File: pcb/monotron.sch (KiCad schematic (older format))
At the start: 29 parts, among them J1 USB_A, J2 USB_B_Micro, J3 SD_Card, J4 Mini-DIN-6, J5 Mini-DIN-6, J6 Conn_02x06_Odd_Even, J7 DB25_Female, J8 DB9_Male, U1 TPS73633DBV, U2 TM4C1231H6PM, Y1 16MHz, Y2 32kHz

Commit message: Added I/O, RS232 and VGA interfaces. Just audio to add.
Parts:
- removed J4, J5: Mini-DIN-6, symbol Connector:Mini-DIN-6
- removed J6: Conn_02x06_Odd_Even, symbol Connector_Generic:Conn_02x06_Odd_Even
- removed J7: DB25_Female, symbol Connector:DB25_Female
- added J5: Conn_02x06_Odd_Even, symbol Connector_Generic:Conn_02x06_Odd_Even
- added J6: DB15_Female_HighDensity_MountingHoles, symbol Connector:DB15_Female_HighDensity_MountingHoles
- added R1, R2, R3: 330, symbol Device:R
- renumbered J8 to J4
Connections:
- net labels added: PA2_SD_CLK, PA3_SD_CS, PA4_SD_MISO, PA5_SD_MOSI, PB4_VGA_HSYNC, PB5_VGA_VSYNC, PB7_VGA_GRN, PD3_VGA_BLU, PE4_AUD_L, PE5_AUD_R, PF1_VGA_RED
- net labels removed: KB_CLK, KB_DATA, MS_CLK, MS_DATA, PA2, PA3, PA4, PA5, PB4, PB5, PB7, PD3, PE4, PE5, PF1, SD_CLK, SD_CS, SD_MISO, SD_MOSI
- wire segments 234 -> 240
- no-connect marks 15 -> 38
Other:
- note added: "TODO! AUDIO OUTPUT GOES HERE"
- note removed: "PS/2 Keyboard"
- note removed: "PS/2 Mouse"
- note removed: "Printer"
- moved on the sheet: J4

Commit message: Changed to use Launchpad instead of bare chip. PS/2 handled by ATTINY24. LPT handled by MCP23017.
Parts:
- removed C1, C10, C17: 1.0u, symbol Device:C
- removed C11: 2.2u, symbol Device:C
- removed C12, C14, C16: 10n, symbol Device:C
- removed C13, C15, C8, C9: 100n, symbol Device:C
- removed C4: 10p, symbol Device:C
- removed C7: 24p, symbol Device:C
- removed J1: USB_A, symbol Connector:USB_A
- removed U1: TPS73633DBV, Package_TO_SOT_SMD:SOT-23-5, symbol Regulator_Linear:TPS73633DBV
- removed U2: TM4C1231H6PM, Package_QFP:LQFP-64_10x10mm_P0.5mm, symbol MCU_Texas:TM4C1231H6PM
- removed Y1: 16MHz, symbol Device:Crystal
- removed Y2: 32kHz, symbol Device:Crystal
- added C2: 10u, symbol Device:C
- added J1: Mono / Stereo, symbol Connector:Conn_01x03_Male
- added J2: AudioJack3, symbol Connector:AudioJack3
- added R1, R2: 150, symbol Device:R
- added R3, R4: 270, symbol Device:R
- added R5, R6: 4.7k, symbol Device:R
- added U2: TM4C123G_Launchpad, symbol tm4c123g_launchpad:TM4C123G_Launchpad
- C3: value 0.01u -> 10u
- C5: value 10p -> 33n
- C6: value 24p -> 33n
- renumbered C2 to C7, J4 to J3, J2 to J4, J3 to J5, J5 to J6, J6 to J7, R1 to R7, R2 to R8, R3 to R9
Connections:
- net labels added: +3V3, PA6_I2C_SCL, PA7_I2C_SDA, PD0_INT_B, PE0_INT_A
- net labels removed: +1V2, PA0, PA1, PA6, PA7, PB2, PB3, PB6, PC0, PC1, PC2, PC3, PD0, PD1, PD2, PD4_USB_DM, PD5_USB_DP, PE0, PE1, PE2, PE3, PE4_AUD_L, PE5_AUD_R, PF0, PF2, PF3, ~HIB, ~RST, ~WAKE
- wire segments 240 -> 145
- no-connect marks 38 -> 31
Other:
- note removed: "TODO! AUDIO OUTPUT GOES HERE"
- note removed: "USB Host Port"
- moved on the sheet: C7, J3, J4, J5, J6, J7, R7, R8, R9

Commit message: Adding footprints.
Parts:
- removed J4: USB_B_Micro, symbol Connector:USB_B_Micro
- added J3: Jack-DC, Connector_BarrelJack:BarrelJack_CUI_PJ-102AH_Horizontal, symbol Connector:Jack-DC
- C1: renamed from C2; footprint (none) -> Capacitor_THT:C_Radial_D5.0mm_H5.0mm_P2.00mm
- C2: renamed from C3; footprint (none) -> Capacitor_THT:C_Radial_D5.0mm_H5.0mm_P2.00mm
- C3: renamed from C7; footprint (none) -> Capacitor_THT:C_Radial_D5.0mm_H5.0mm_P2.00mm
- C4: renamed from C5; footprint (none) -> Capacitor_THT:C_Disc_D5.0mm_W2.5mm_P2.50mm
- C5: renamed from C6; footprint (none) -> Capacitor_THT:C_Disc_D5.0mm_W2.5mm_P2.50mm
- J1: footprint (none) -> Connector_PinHeader_2.54mm:PinHeader_1x03_P2.54mm_Vertical; Digikey (none) -> 609-3504-ND‎
- J4: renamed from J3; footprint (none) -> Connector_Dsub:DSUB-9_Male_Horizontal_P2.77x2.84mm_EdgePinOffset7.70mm_Housed_MountingHolesOffset9.12mm; Digikey (none) -> 609-5918-ND
- J5: footprint (none) -> Connector_Card:SD_TE_2041021; Digikey (none) -> A130907-ND‎
- J6: footprint (none) -> Connector_PinHeader_2.54mm:PinHeader_2x06_P2.54mm_Vertical; Digikey (none) -> 609-3263-ND‎
- J7: footprint (none) -> Connector_Dsub:DSUB-15-HD_Female_Horizontal_P2.29x1.98mm_EdgePinOffset8.35mm_Housed_MountingHolesOffset10.89mm; Digikey (none) -> 609-5181-ND
- R1, R2, R3, R4, R5, R6, R7, R8, R9: footprint (none) -> Resistor_THT:R_Axial_DIN0411_L9.9mm_D3.6mm_P12.70mm_Horizontal
- U1: renamed from U2; footprint (none) -> Launchpad:Launchpad_4x10
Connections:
- no-connect marks 31 -> 27
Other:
- moved on the sheet: C3

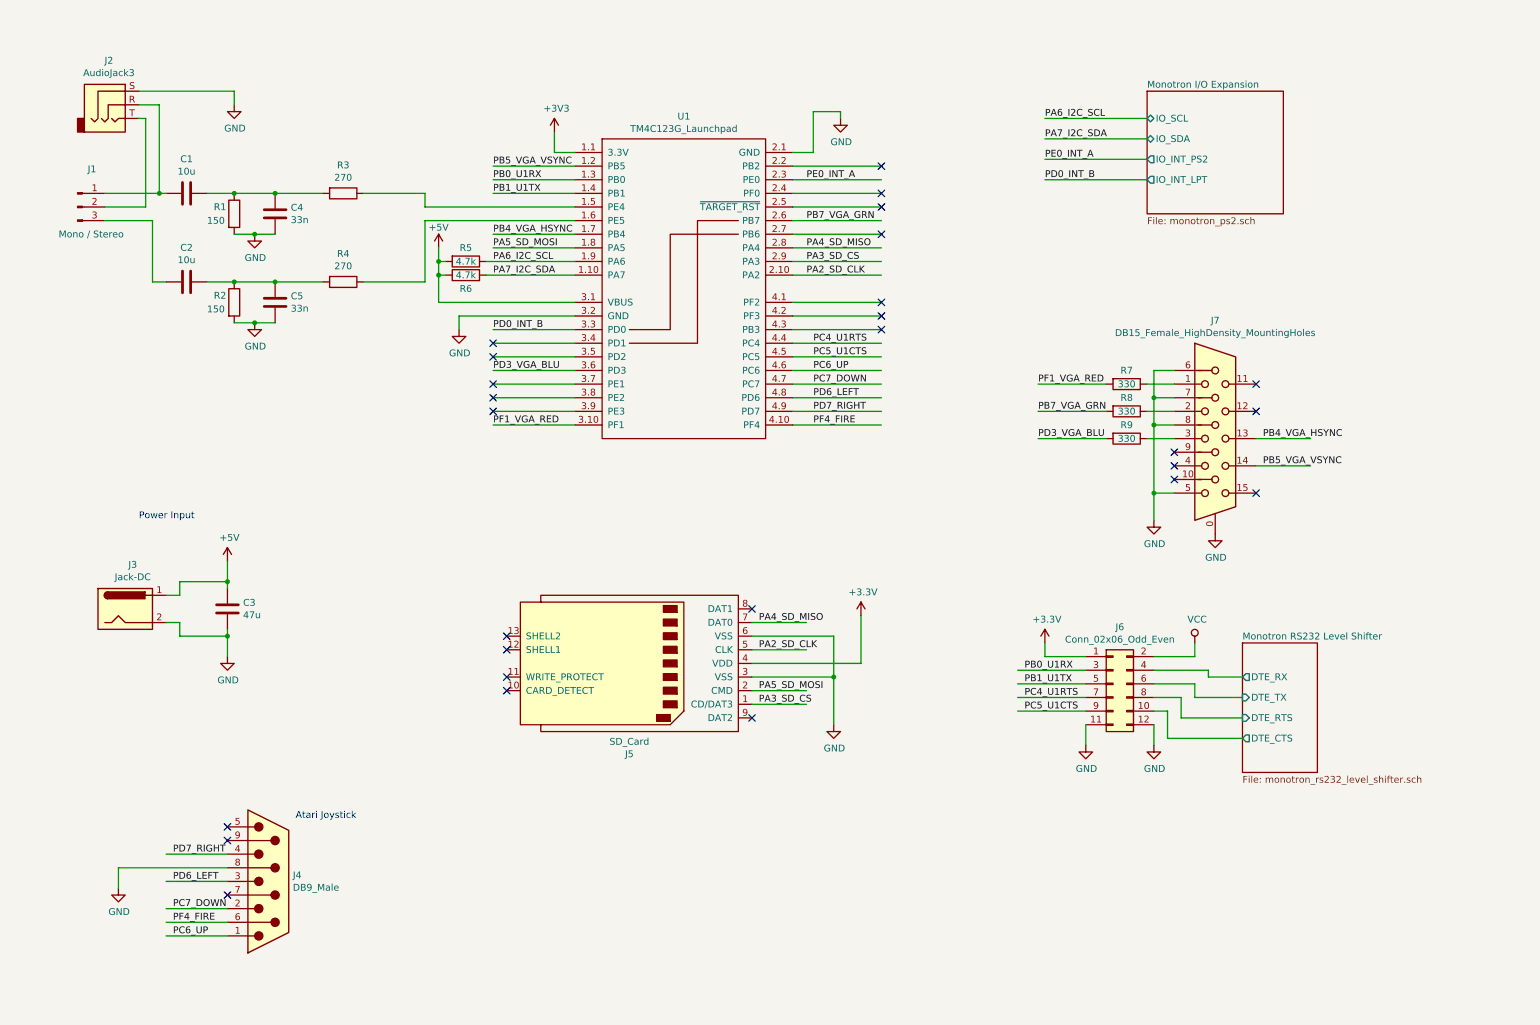
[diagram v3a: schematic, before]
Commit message: Added footprints. Change SD footprint for breakout board. Changed PS2/LPT interface to single AtMega48A. Moved MAX3232 to main sheet. Added I2C header. Started PCB layout.
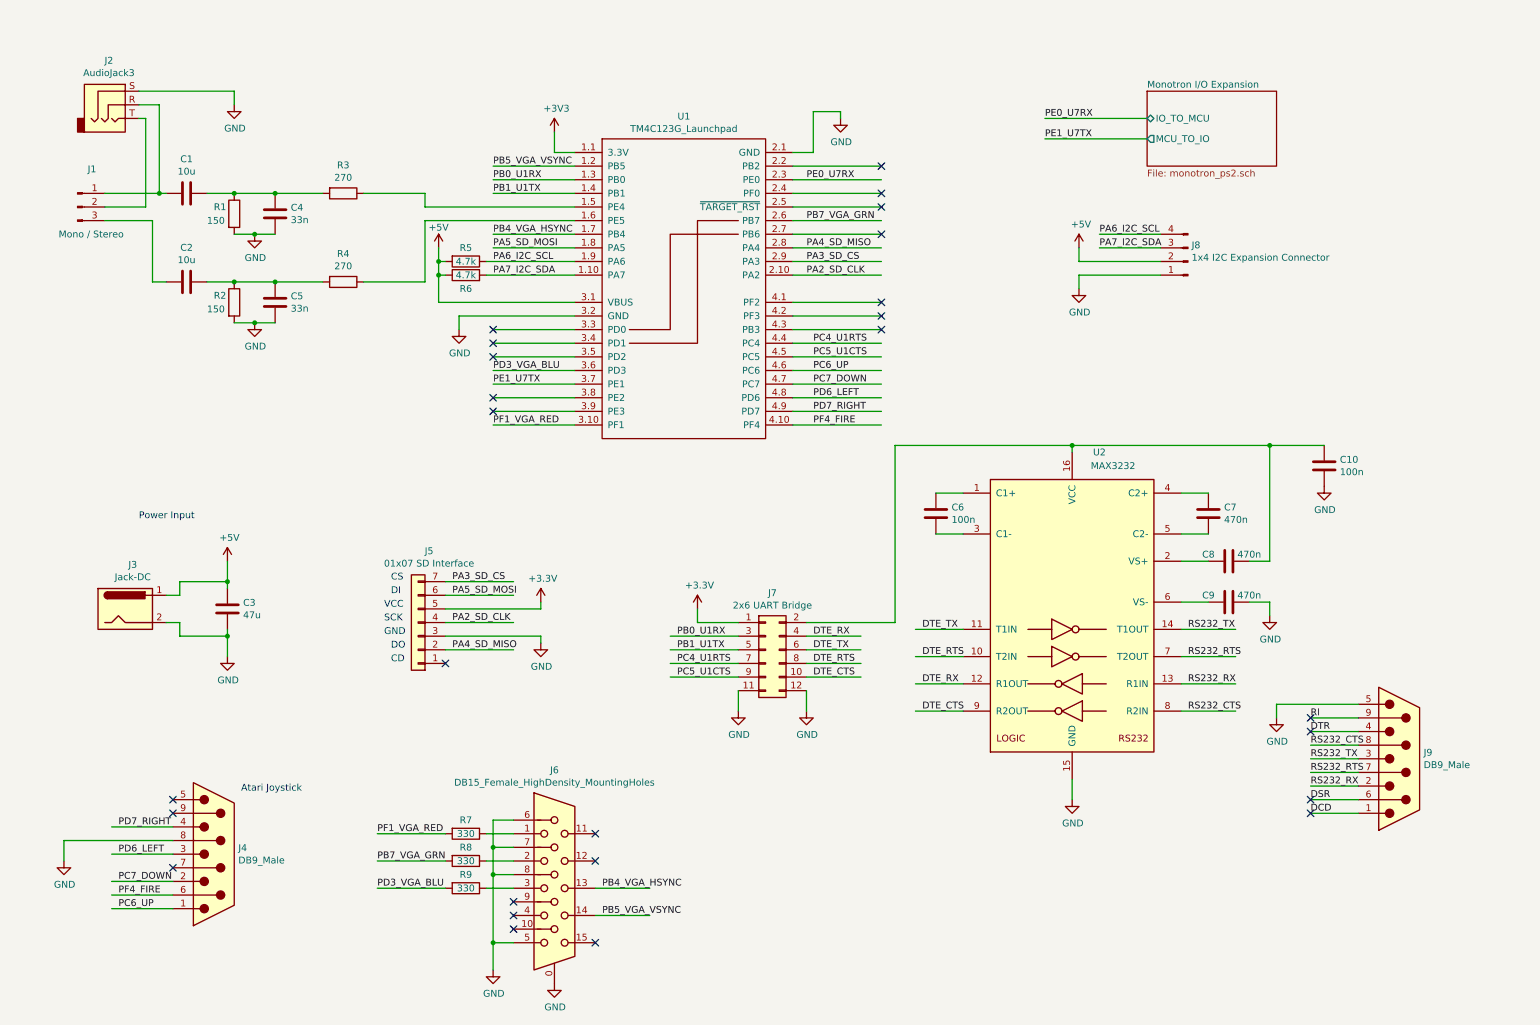
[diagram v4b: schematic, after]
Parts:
- removed J5: SD_Card, Connector_Card:SD_TE_2041021, symbol Connector:SD_Card
- added C10, C6: 100n, Capacitor_THT:C_Disc_D5.0mm_W2.5mm_P2.50mm, symbol Device:C
- added C7, C8, C9: 470n, Capacitor_THT:C_Disc_D5.0mm_W2.5mm_P2.50mm, symbol Device:C
- added J5: 01x07 SD Interface, Connector_PinHeader_2.54mm:PinHeader_1x07_P2.54mm_Vertical, symbol Connector_Generic:Conn_01x07
- added J8: 1x4 I2C Expansion Connector, Connector_PinHeader_2.54mm:PinHeader_1x04_P2.54mm_Vertical, symbol Connector:Conn_01x04_Male
- added J9: DB9_Male, Connector_Dsub:DSUB-9_Male_Horizontal_P2.77x2.84mm_EdgePinOffset7.70mm_Housed_MountingHolesOffset9.12mm, symbol Connector:DB9_Male
- added U2: MAX3232, Package_DIP:DIP-16_W7.62mm, symbol Interface_UART:MAX3232
- J2: footprint (none) -> Connector_Audio:Jack_3.5mm_CUI_SJ1-3533NG_Horizontal
- J7: renamed from J6; value Conn_02x06_Odd_Even -> 2x6 UART Bridge
- U1: Digikey (none) -> 296-35760-ND
- renumbered J7 to J6
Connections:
- net labels added: DCD, DSR, DTE_CTS, DTE_RTS, DTE_RX, DTE_TX, DTR, PE0_U7RX, PE1_U7TX, RI, RS232_CTS, RS232_RTS, RS232_RX, RS232_TX
- net labels removed: PD0_INT_B, PE0_INT_A, VCC
- wire segments 145 -> 172
- no-connect marks 27 -> 26
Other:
- note added: "CD"
- note added: "CS"
- note added: "DI"
- note added: "DO"
- note added: "GND"
- note added: "SCK"
- note added: "VCC"
- moved on the sheet: J4, J6, J7, R7, R8, R9

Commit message: Added MIDI interface.
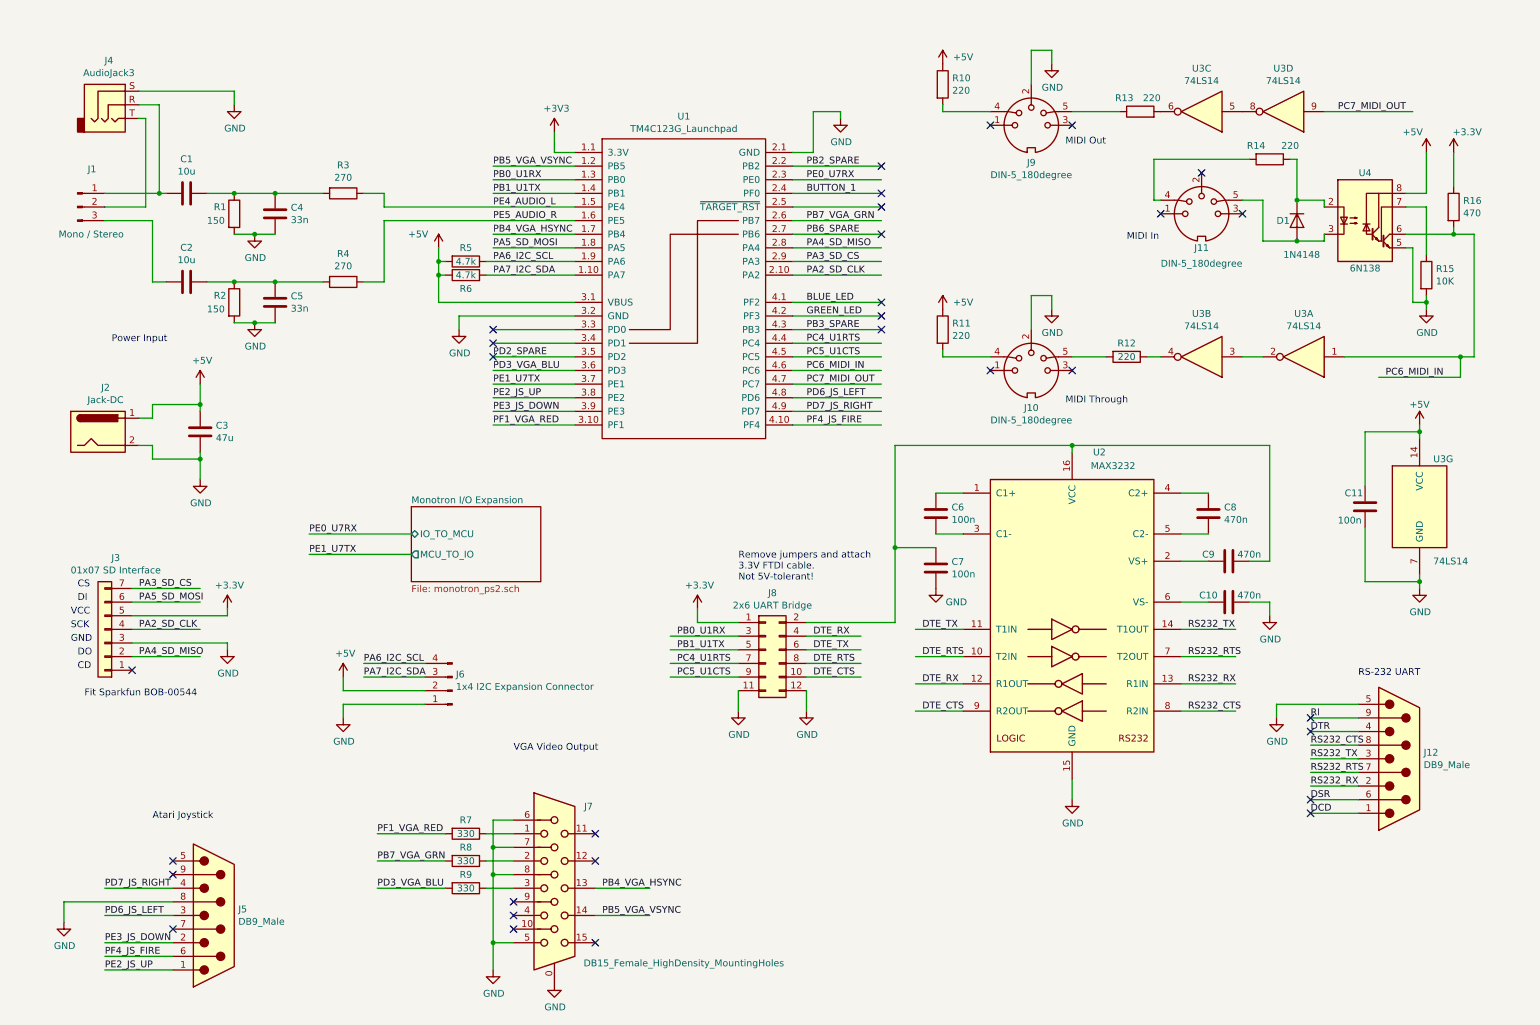
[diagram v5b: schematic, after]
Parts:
- added C11: 100n, Capacitor_THT:C_Disc_D5.0mm_W2.5mm_P2.50mm, symbol Device:C
- added D1: 1N4148, symbol Device:D
- added J10, J11, J9: DIN-5_180degree, symbol Connector:DIN-5_180degree
- added R10, R11, R12, R13, R14: 220, symbol Device:R
- added R15: 10K, symbol Device:R
- added R16: 470, symbol Device:R
- added U3: 74LS14, symbol 74xx:74LS14
- added U4: 6N138, symbol Isolator:6N138
- renumbered C9 to C10, C10 to C7, C7 to C8, C8 to C9, J9 to J12, J3 to J2, J5 to J3, J2 to J4, J4 to J5, J8 to J6, J6 to J7, J7 to J8
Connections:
- net labels added: BLUE_LED, BUTTON_1, GREEN_LED, PB2_SPARE, PB3_SPARE, PB6_SPARE, PC6_MIDI_IN, PC7_MIDI_OUT, PD2_SPARE, PD6_JS_LEFT, PD7_JS_RIGHT, PE2_JS_UP, PE3_JS_DOWN, PE4_AUDIO_L, PE5_AUDIO_R, PF4_JS_FIRE
- net labels removed: PC6_UP, PC7_DOWN, PD6_LEFT, PD7_RIGHT, PF4_FIRE
- wire segments 172 -> 226
- no-connect marks 26 -> 31
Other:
- note added: "Fit Sparkfun BOB-00544"
- note added: "MIDI In"
- note added: "MIDI Out"
- note added: "MIDI Through"
- note added: "RS-232 UART"
- note added: "Remove jumpers and attach\n3.3V FTDI cable.\nNot 5V-tolerant!"
- note added: "VGA Video Output"
- moved on the sheet: C3, C7, J2, J3, J5, J6
